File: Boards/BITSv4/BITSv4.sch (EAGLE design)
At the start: 32 parts, among them U1 LMR16020, X1 53261-10

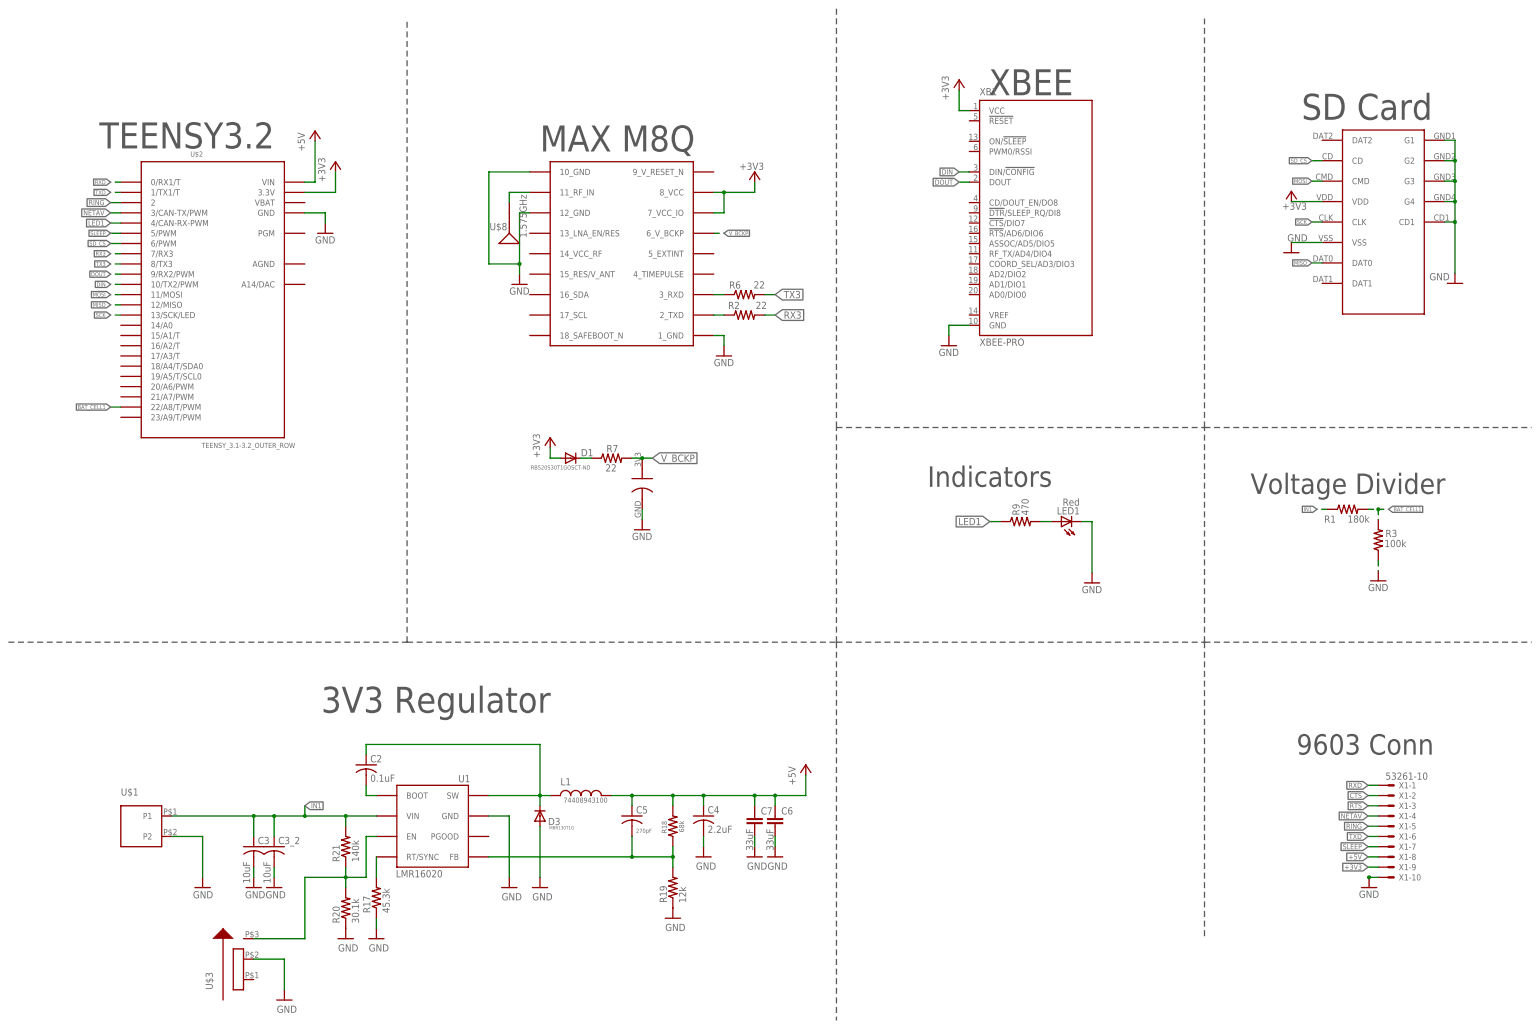
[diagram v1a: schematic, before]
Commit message: connector move
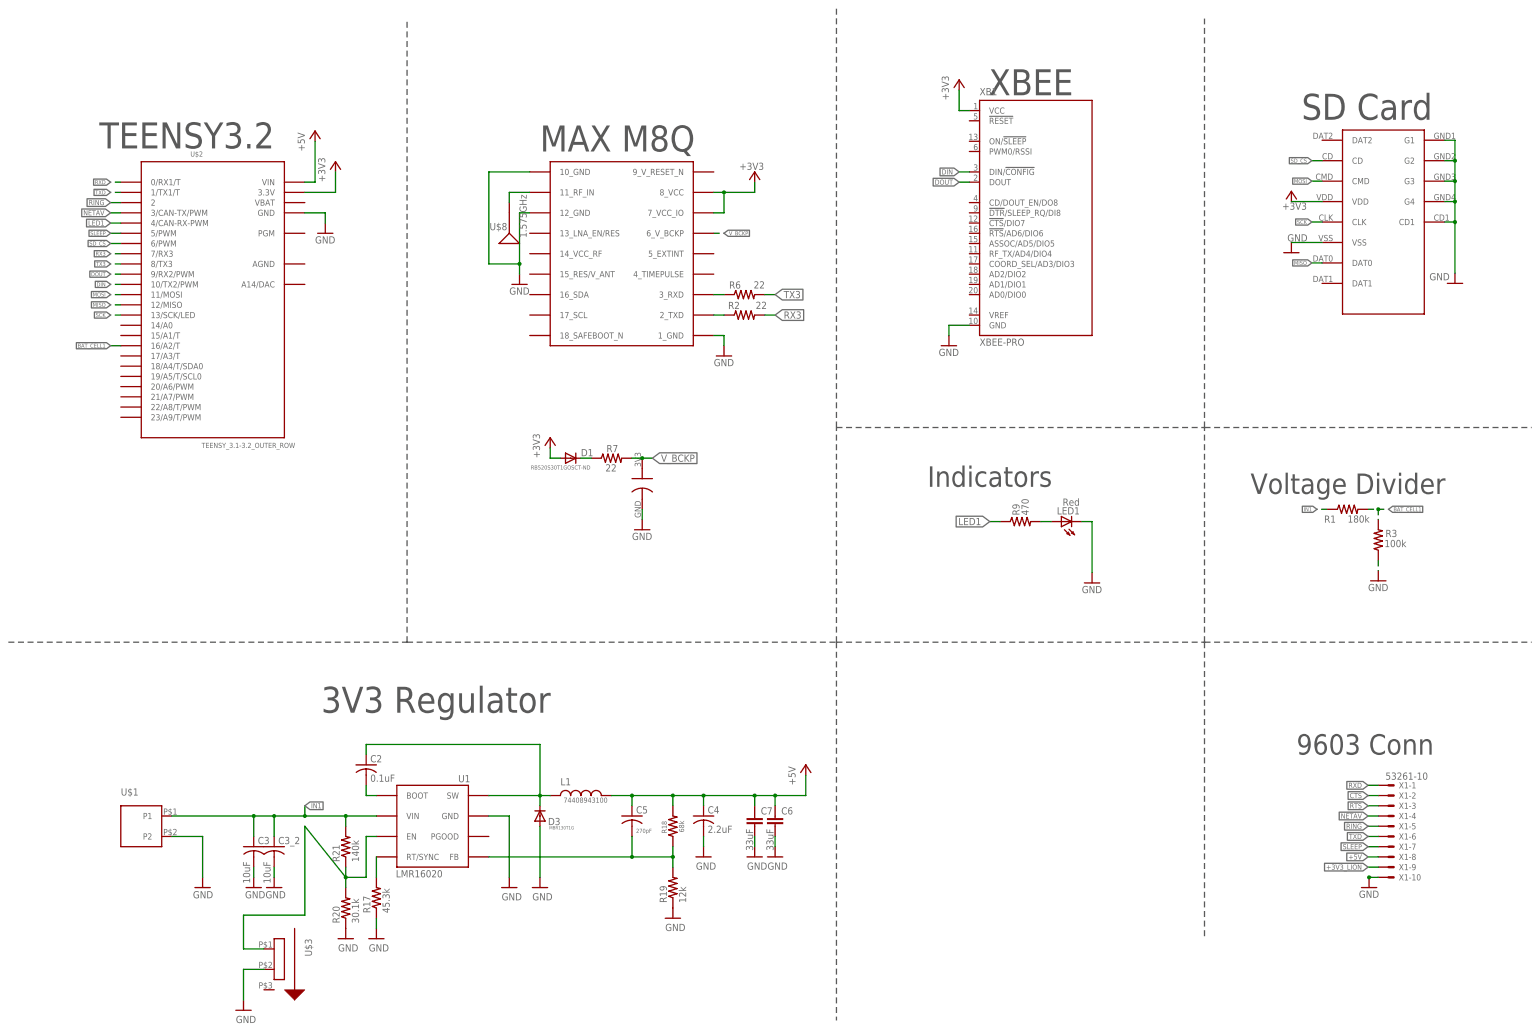
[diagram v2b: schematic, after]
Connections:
- new net +3V3_LION: X1-9.S
- net +3V3: no longer X1-9.S
- net BAT_CELL1: now also U$2.16/A2/T; no longer U$2.22/A8/T/PWM
- net N$7: now also U$3.P1; no longer U$3.P3
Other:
- moved on the sheet: U$3
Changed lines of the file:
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@@
 <attribute name="NAME" x="33.02" y="144.78" size="1.778" layer="95"/>
 </instance>
-<instance part="U$3" gate="G$1" x="68.58" y="104.14" smashed="yes" rot="R90">
-<attribute name="NAME" x="55.88" y="96.52" size="1.778" layer="95" rot="R90"/>
-</instance>
-<instance part="SUPPLY10" gate="1" x="73.66" y="93.98" smashed="yes">
-<attribute name="VALUE" x="71.755" y="90.805" size="1.778" layer="96"/>
+<instance part="U$3" gate="G$1" x="66.04" y="101.6" smashed="yes" rot="R270">
+<attribute name="NAME" x="78.74" y="109.22" size="1.778" layer="95" rot="R270"/>
+</instance>
+<instance part="SUPPLY10" gate="1" x="63.5" y="91.44" smashed="yes">
+<attribute name="VALUE" x="61.595" y="88.265" size="1.778" layer="96"/>
 </instance>
 <instance part="L1" gate="G$1" x="139.7" y="144.78" smashed="yes">
@@
 </segment>
 <segment>
+<pinref part="SUPPLY10" gate="1" pin="GND"/>
 <pinref part="U$3" gate="G$1" pin="P2"/>
-<wire x1="66.04" y1="104.14" x2="73.66" y2="104.14" width="0.1524" layer="91"/>
-<wire x1="73.66" y1="104.14" x2="73.66" y2="96.52" width="0.1524" layer="91"/>
-<pinref part="SUPPLY10" gate="1" pin="GND"/>
+<wire x1="63.5" y1="93.98" x2="63.5" y2="101.6" width="0.1524" layer="91"/>
+<wire x1="63.5" y1="101.6" x2="68.58" y2="101.6" width="0.1524" layer="91"/>
 </segment>
 <segment>
@@
 <wire x1="182.88" y1="294.64" x2="190.5" y2="294.64" width="0.1524" layer="91"/>
 <junction x="182.88" y="294.64"/>
-</segment>
-<segment>
-<pinref part="X1" gate="-9" pin="S"/>
-<wire x1="345.44" y1="127" x2="342.9" y2="127" width="0.1524" layer="91"/>
-<label x="342.9" y="127" size="1.27" layer="95" rot="R180" xref="yes"/>
 </segment>
 </net>
@@
 </segment>
 <segment>
-<pinref part="U$2" gate="G$1" pin="22/A8/T/PWM"/>
-<wire x1="33.02" y1="241.3" x2="30.48" y2="241.3" width="0.1524" layer="91"/>
-<label x="30.48" y="241.3" size="1.016" layer="95" rot="R180" xref="yes"/>
+<label x="30.48" y="256.54" size="1.016" layer="95" rot="R180" xref="yes"/>
+<pinref part="U$2" gate="G$1" pin="16/A2/T"/>
+<wire x1="33.02" y1="256.54" x2="30.48" y2="256.54" width="0.1524" layer="91"/>
 </segment>
 </net>
@@
 <net name="N$7" class="0">
 <segment>
-<pinref part="U$3" gate="G$1" pin="P3"/>
-<wire x1="66.04" y1="109.22" x2="78.74" y2="109.22" width="0.1524" layer="91"/>
 <pinref part="R21" gate="G$1" pin="1"/>
 <wire x1="88.9" y1="124.46" x2="88.9" y2="127" width="0.1524" layer="91"/>
@@
 <pinref part="R20" gate="G$1" pin="2"/>
 <wire x1="88.9" y1="121.92" x2="88.9" y2="124.46" width="0.1524" layer="91"/>
-<wire x1="78.74" y1="109.22" x2="78.74" y2="124.46" width="0.1524" layer="91"/>
-<wire x1="78.74" y1="124.46" x2="88.9" y2="124.46" width="0.1524" layer="91"/>
-</segment>
-</net>
+<wire x1="78.74" y1="115.062" x2="78.74" y2="137.16" width="0.1524" layer="91"/>
+<wire x1="78.74" y1="137.16" x2="88.9" y2="124.46" width="0.1524" layer="91"/>
+<wire x1="63.5" y1="115.062" x2="78.74" y2="115.062" width="0.1524" layer="91"/>
+<pinref part="U$3" gate="G$1" pin="P1"/>
+<wire x1="68.58" y1="106.68" x2="63.5" y2="106.68" width="0.1524" layer="91"/>
+<wire x1="63.5" y1="106.68" x2="63.5" y2="115.062" width="0.1524" layer="91"/>
+</segment>
+</net>
+<net name="+3V3_LION" class="0">
+<segment>
+<pinref part="X1" gate="-9" pin="S"/>
+<wire x1="345.44" y1="127" x2="342.9" y2="127" width="0.1524" layer="91"/>
+<label x="342.9" y="127" size="1.27" layer="95" rot="R180" xref="yes"/>
+</segment>
+</net>
